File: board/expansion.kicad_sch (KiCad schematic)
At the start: 1 part, among them J7 Conn_02x32_Counter_Clockwise

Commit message: design draft complete, added footprints
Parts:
- J7: footprint (none) -> Connector_PinHeader_2.54mm:PinHeader_2x32_P2.54mm_Vertical
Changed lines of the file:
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@@
 			)
 		)
-		(property "Footprint" ""
+		(property "Footprint" "Connector_PinHeader_2.54mm:PinHeader_2x32_P2.54mm_Vertical"
 			(at 97.79 73.66 0)
 			(effects

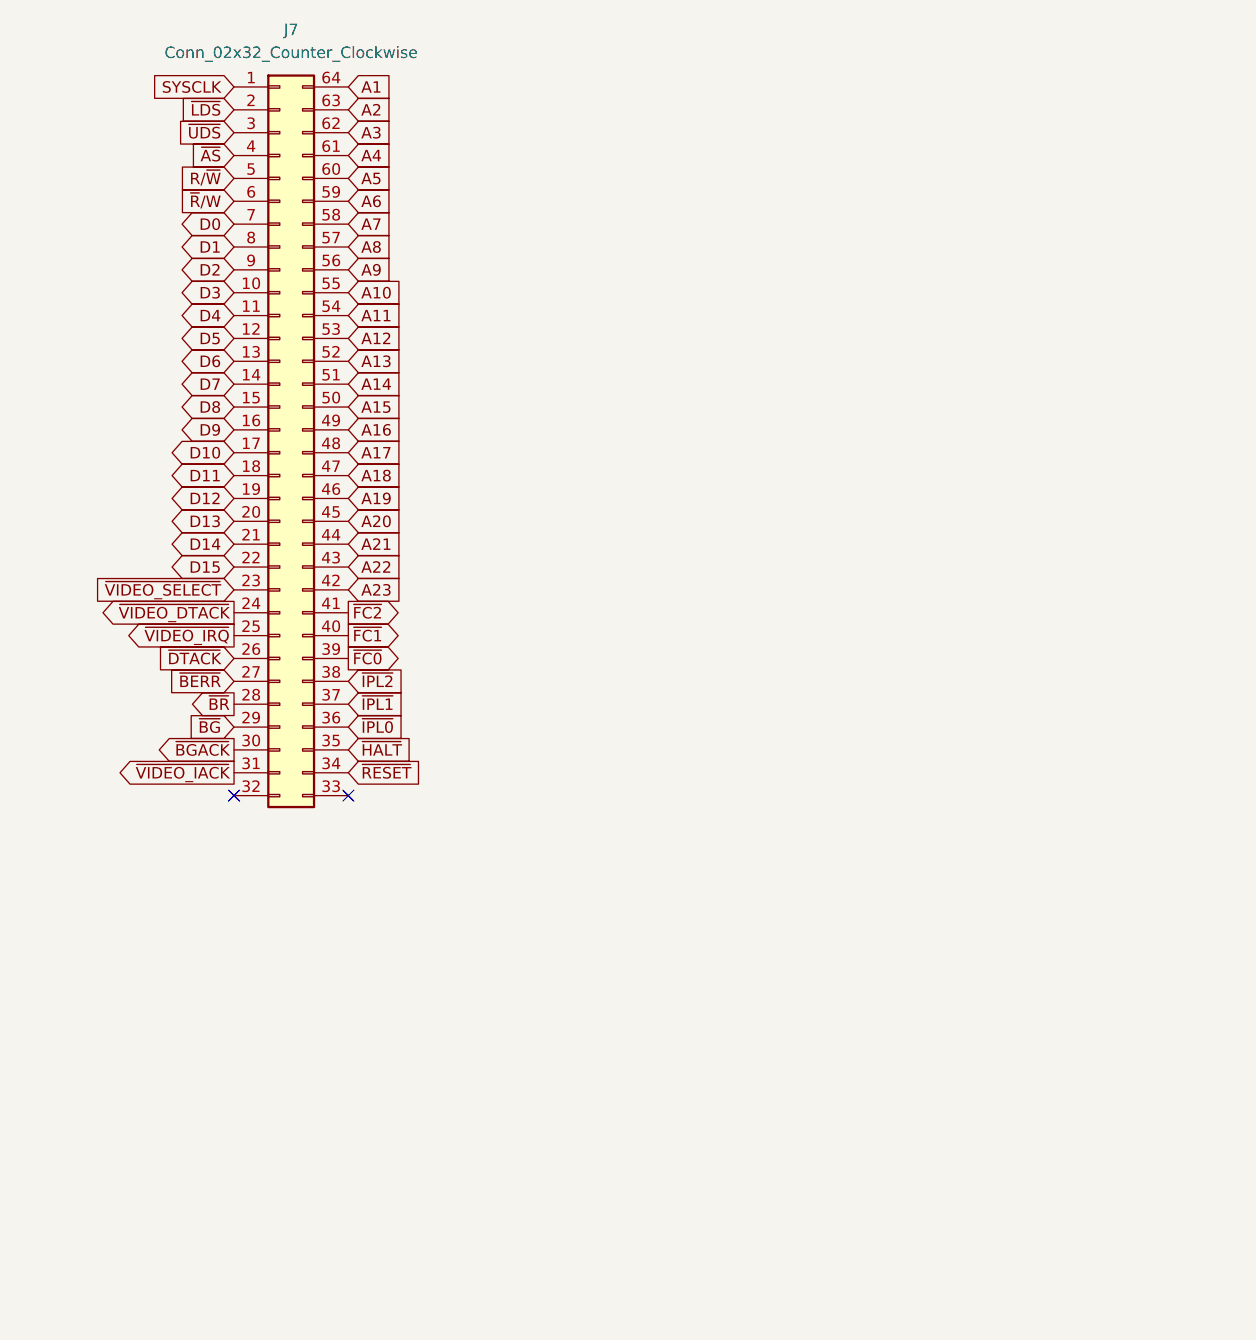
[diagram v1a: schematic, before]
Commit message: start of PCB and MMU
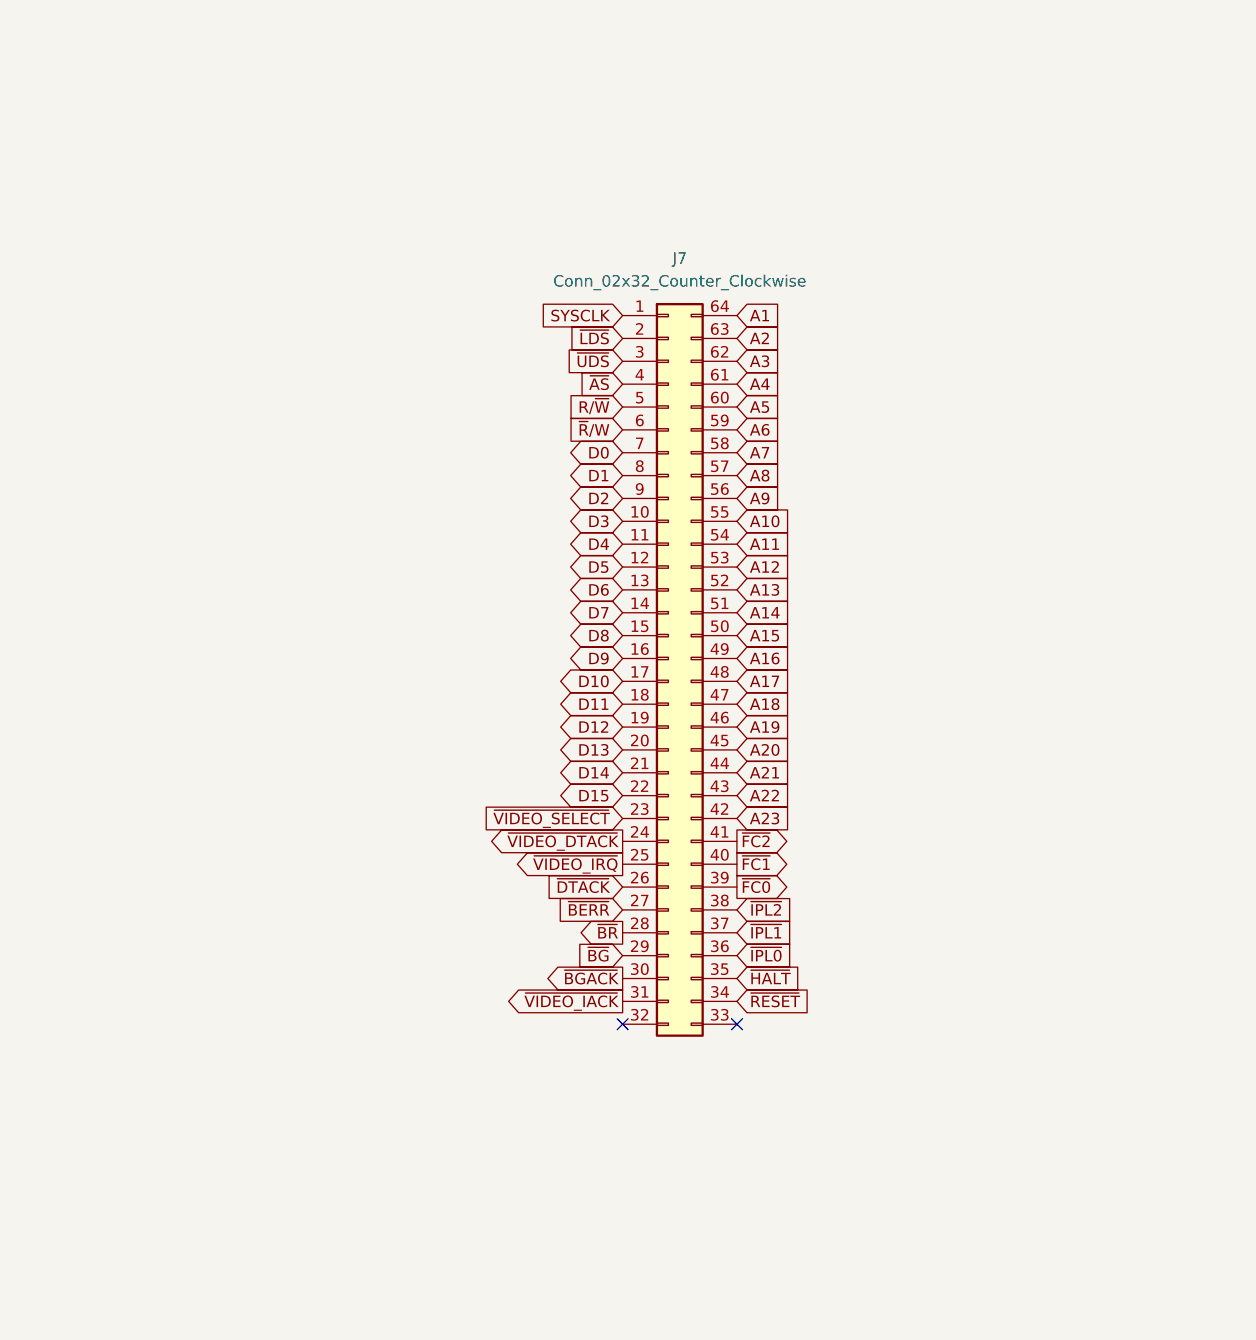
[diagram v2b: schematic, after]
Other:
- moved on the sheet: J7

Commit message: checkpoint
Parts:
- added H5, H6, H7, H8: MountingHole_Pad, MountingHole:MountingHole_2.5mm_Pad, symbol Mechanical:MountingHole_Pad
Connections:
- new net GND: H5.1, H6.1, H7.1, H8.1

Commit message: checkpoint - maybe unfinishable
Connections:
- net VIDEO_PRESENT: now reaches J7.32 (Pin_32)
- no-connect marks 2 -> 1
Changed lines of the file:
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@@
 		(at 148.59 139.7)
-	)
-	(no_connect
-		(at 135.89 139.7)
 	)
 	(global_label "D2"
@@
 				(hide yes)
 			)
+		)
+	)
+	(global_label "VIDEO_PRESENT"
+		(shape output)
+		(at 135.89 139.7 180)
+		(fields_autoplaced yes)
+		(effects
+			(font
+				(size 1.27 1.27)
+			)
+			(justify right)
+		)
+		(property "Intersheetrefs" "${INTERSHEET_REFS}"
+			(at 118.1487 139.7 0)
+			(effects
+				(font
+					(size 1.27 1.27)
+				)
+				(justify right)
+				(hide yes)
+			)

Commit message: checkpoint before reordering 1508 inputs
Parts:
- removed H5, H8: MountingHole_Pad, MountingHole:MountingHole_2.5mm_Pad, symbol Mechanical:MountingHole_Pad
- H6, H7: footprint MountingHole:MountingHole_2.5mm_Pad -> MountingHole:MountingHole_2.5mm_Pad_Via
- J7: value Conn_02x32_Counter_Clockwise -> Expansion Bus; footprint Connector_PinHeader_2.54mm:PinHeader_2x32_P2.54mm_Vertical -> Connector_PinHeader_2.54mm:PinHeader_2x36_P2.54mm_Vertical; symbol Connector_Generic:Conn_02x32_Counter_Clockwise -> Connector_Generic:Conn_02x36_Odd_Even
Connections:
- net A1: now also J7.53 (Pin_53); no longer J7.64 (Pin_64)
- net A10: now also J7.56 (Pin_56); no longer J7.55 (Pin_55)
- net A12: now also J7.52 (Pin_52); no longer J7.53 (Pin_53)
- net A13: now also J7.50 (Pin_50); no longer J7.52 (Pin_52)
- net A14: now also J7.48 (Pin_48); no longer J7.51 (Pin_51)
- net A15: now also J7.46 (Pin_46); no longer J7.50 (Pin_50)
- net A16: now also J7.44 (Pin_44); no longer J7.49 (Pin_49)
- net A17: now also J7.42 (Pin_42); no longer J7.48 (Pin_48)
- net A18: now also J7.40 (Pin_40); no longer J7.47 (Pin_47)
- net A19: now also J7.38 (Pin_38); no longer J7.46 (Pin_46)
- net A2: now also J7.55 (Pin_55); no longer J7.63 (Pin_63)
- net A20: now also J7.36 (Pin_36); no longer J7.45 (Pin_45)
- net A21: now also J7.32 (Pin_32); no longer J7.44 (Pin_44)
- net A22: now also J7.30 (Pin_30); no longer J7.43 (Pin_43)
- net A23: now also J7.28 (Pin_28); no longer J7.42 (Pin_42)
- net A3: now also J7.57 (Pin_57); no longer J7.62 (Pin_62)
- net A4: now also J7.59 (Pin_59); no longer J7.61 (Pin_61)
- net A5: now also J7.66 (Pin_66); no longer J7.60 (Pin_60)
- net A6: now also J7.64 (Pin_64); no longer J7.59 (Pin_59)
- net A7: now also J7.62 (Pin_62); no longer J7.58 (Pin_58)
- net A8: now also J7.60 (Pin_60); no longer J7.57 (Pin_57)
- net A9: now also J7.58 (Pin_58); no longer J7.56 (Pin_56)
- net D0: now also J7.11 (Pin_11); no longer J7.7 (Pin_7)
- net D1: now also J7.9 (Pin_9); no longer J7.8 (Pin_8)
- net D10: now also J7.14 (Pin_14); no longer J7.17 (Pin_17)
- net D11: now also J7.16 (Pin_16); no longer J7.18 (Pin_18)
- net D12: now also J7.18 (Pin_18); no longer J7.19 (Pin_19)
- net D14: now also J7.22 (Pin_22); no longer J7.21 (Pin_21)
- net D15: now also J7.24 (Pin_24); no longer J7.22 (Pin_22)
- net D2: now also J7.7 (Pin_7); no longer J7.9 (Pin_9)
- net D3: now also J7.5 (Pin_5); no longer J7.10 (Pin_10)
- net D4: now also J7.3 (Pin_3); no longer J7.11 (Pin_11)
- net D5: now also J7.4 (Pin_4); no longer J7.12 (Pin_12)
- net D6: now also J7.6 (Pin_6); no longer J7.13 (Pin_13)
- net D7: now also J7.8 (Pin_8); no longer J7.14 (Pin_14)
- net D8: now also J7.10 (Pin_10); no longer J7.15 (Pin_15)
- net D9: now also J7.12 (Pin_12); no longer J7.16 (Pin_16)
- net GND: now also J7.26 (Pin_26), J7.33 (Pin_33)
- net R/~{W}: now also J7.19 (Pin_19); no longer J7.5 (Pin_5)
- net SYSCLK: now also J7.31 (Pin_31); no longer J7.1 (Pin_1)
- net VIDEO_PRESENT: now also J7.70 (Pin_70); no longer J7.32 (Pin_32)
- net ~{AS}: now also J7.13 (Pin_13); no longer J7.4 (Pin_4)
- net ~{BERR}: now also J7.39 (Pin_39); no longer J7.27 (Pin_27)
- net ~{BGACK}: now also J7.25 (Pin_25); no longer J7.30 (Pin_30)
- net ~{BG}: now also J7.23 (Pin_23); no longer J7.29 (Pin_29)
- net ~{BR}: now also J7.27 (Pin_27); no longer J7.28 (Pin_28)
- net ~{DTACK}: now also J7.67 (Pin_67); no longer J7.26 (Pin_26)
- net ~{FC0}: now also J7.51 (Pin_51); no longer J7.39 (Pin_39)
- net ~{FC1}: now also J7.49 (Pin_49); no longer J7.40 (Pin_40)
- net ~{FC2}: now also J7.47 (Pin_47); no longer J7.41 (Pin_41)
- net ~{IPL0}: now also J7.45 (Pin_45); no longer J7.36 (Pin_36)
- net ~{IPL1}: now also J7.43 (Pin_43); no longer J7.37 (Pin_37)
- net ~{IPL2}: now also J7.41 (Pin_41); no longer J7.38 (Pin_38)
- net ~{LDS}: now also J7.17 (Pin_17); no longer J7.2 (Pin_2)
- net ~{RESET}: now also J7.37 (Pin_37); no longer J7.34 (Pin_34)
- net ~{R}/W: now also J7.21 (Pin_21); no longer J7.6 (Pin_6)
- net ~{UDS}: now also J7.15 (Pin_15); no longer J7.3 (Pin_3)
- net ~{VIDEO_DTACK}: now also J7.63 (Pin_63); no longer J7.24 (Pin_24)
- net ~{VIDEO_IACK}: now also J7.68 (Pin_68); no longer J7.31 (Pin_31)
- net ~{VIDEO_IRQ}: now also J7.65 (Pin_65); no longer J7.25 (Pin_25)
- net ~{VIDEO_SELECT}: now also J7.61 (Pin_61); no longer J7.23 (Pin_23)
- new net +3V3: J7.1 (Pin_1), J7.2 (Pin_2)
- new net +5V: J7.29 (Pin_29), J7.34 (Pin_34)
- no-connect marks 1 -> 3

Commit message: CF card, composite, VGA
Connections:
- net +3V3: no longer names the net of J7.1 (Pin_1)
- net +3V3: no longer J7.2 (Pin_2)
- no-connect marks 3 -> 5
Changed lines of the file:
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@@
+	)
+	(no_connect
+		(at 125.73 48.26)
+	)
+	(no_connect
+		(at 113.03 48.26)
 	)
 	(no_connect
@@
 	(wire
 		(pts
-			(xy 99.06 48.26) (xy 113.03 48.26)
+			(xy 96.52 88.9) (xy 113.03 88.9)
 		)
 		(stroke
@@
 	(wire
 		(pts
-			(xy 96.52 88.9) (xy 113.03 88.9)
+			(xy 96.52 83.82) (xy 113.03 83.82)
 		)
 		(stroke
@@
 	(wire
 		(pts
-			(xy 96.52 83.82) (xy 113.03 83.82)
-		)
-		(stroke
-			(width 0)
-			(type default)
-		)
-	)
-	(wire
-		(pts
 			(xy 125.73 88.9) (xy 146.05 88.9)
-		)
-		(stroke
-			(width 0)
-			(type default)
-		)
-	)
-	(wire
-		(pts
-			(xy 125.73 48.26) (xy 137.16 48.26)
 		)
 		(stroke
@@
 	)
 	(symbol
-		(lib_id "power:+3V3")
-		(at 137.16 48.26 0)
-		(unit 1)
-		(exclude_from_sim no)
-		(in_bom yes)
-		(on_board yes)
-		(dnp no)
-		(fields_autoplaced yes)
-		(property "Reference" "#PWR0167"
-			(at 137.16 52.07 0)
-			(effects
-				(font
-					(size 1.27 1.27)
-				)
-				(hide yes)
-			)
-		)
-		(property "Value" "+3V3"
-			(at 137.16 43.18 0)
-			(effects
-				(font
-					(size 1.27 1.27)
-				)
-			)
-		)
-		(property "Footprint" ""
-			(at 137.16 48.26 0)
-			(effects
-				(font
-					(size 1.27 1.27)
-				)
-				(hide yes)
-			)
-		)
-		(property "Datasheet" ""
-			(at 137.16 48.26 0)
-			(effects
-				(font
-					(size 1.27 1.27)
-				)
-				(hide yes)
-			)
-		)
-		(property "Description" "Power symbol creates a global label with name \"+3V3\""
-			(at 137.16 48.26 0)
-			(effects
-				(font
-					(size 1.27 1.27)
-				)
-				(hide yes)
-			)
-		)
-		(pin "1"
-		)
-		(instances
-			(project "board"
-				(path "/afefa398-9f39-4b22-97f8-dae9b102df0d/a6ee04b7-7d16-47ea-9db5-ea25e69d73a5"
-					(reference "#PWR0167")
-					(unit 1)
-				)
-			)
-		)
-	)
-	(symbol
 		(lib_id "Mechanical:MountingHole_Pad")
 		(at 193.04 88.9 90)
@@
 					(unit 1)
 				)
-			)
-		)
-	)
-	(symbol
-		(lib_id "power:+3V3")
-		(at 99.06 48.26 0)
-		(unit 1)
-		(exclude_from_sim no)
-		(in_bom yes)
-		(on_board yes)
-		(dnp no)
-		(fields_autoplaced yes)
-		(property "Reference" "#PWR0166"
-			(at 99.06 52.07 0)
-			(effects
-				(font
-					(size 1.27 1.27)
-				)
-				(hide yes)
-			)
-		)
-		(property "Value" "+3V3"
-			(at 99.06 43.18 0)
-			(effects
-				(font
-					(size 1.27 1.27)
-				)
-			)
-		)
-		(property "Footprint" ""
-			(at 99.06 48.26 0)
-			(effects
-				(font
-					(size 1.27 1.27)
-				)
-				(hide yes)
-			)
-		)
-		(property "Datasheet" ""
-			(at 99.06 48.26 0)
-			(effects
-				(font
-					(size 1.27 1.27)
-				)
-				(hide yes)
-			)
-		)
-		(property "Description" "Power symbol creates a global label with name \"+3V3\""
-			(at 99.06 48.26 0)
-			(effects
-				(font
-					(size 1.27 1.27)
-				)
-				(hide yes)
-			)
-		)
-		(pin "1"
-		)
-		(instances
-			(project ""
-				(path "/afefa398-9f39-4b22-97f8-dae9b102df0d/a6ee04b7-7d16-47ea-9db5-ea25e69d73a5"
-					(reference "#PWR0166")
-					(unit 1)
-				)

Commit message: checkpoint
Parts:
- removed H6, H7: MountingHole_Pad, MountingHole:MountingHole_2.5mm_Pad_Via, symbol Mechanical:MountingHole_Pad
- removed J7: Expansion Bus, Connector_PinHeader_2.54mm:PinHeader_2x36_P2.54mm_Vertical, symbol Connector_Generic:Conn_02x36_Odd_Even
- added C18: 100nF, Capacitor_THT:C_Disc_D5.0mm_W2.5mm_P5.00mm, symbol Device:C
- added U13: ENGINE, Package_LCC:PLCC-84_THT-Socket, symbol CPLD_Microchip:ATF1508ASx-xxJx84
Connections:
- net +5V: now also C18.1, U13.13 (VCCIO), U13.26 (VCCIO), U13.3 (VCCINT), U13.38 (VCCIO), U13.43 (VCCINT), U13.53 (VCCIO), U13.66 (VCCIO), U13.78 (VCCIO)
- net A1: now also U13.48 (I/O)
- net A10: now also U13.39 (I/O)
- net A11: now also U13.37 (I/O)
- net A13: now also U13.36 (I/O)
- net A14: now also U13.75 (I/O)
- net A15: now also U13.74 (I/O)
- net A16: now also U13.56 (I/O)
- net A17: now also U13.57 (I/O)
- net A18: now also U13.31 (I/O)
- net A19: now also U13.30 (I/O)
- net A2: now also U13.49 (I/O)
- net A20: now also U13.58 (I/O)
- net A21: now also U13.28 (I/O)
- net A22: now also U13.60 (I/O)
- net A23: now also U13.61 (I/O)
- net A3: now also U13.51 (I/O)
- net A4: now also U13.54 (I/O)
- net A5: now also U13.55 (I/O)
- net A6: now also U13.52 (I/O)
- net A7: now also U13.50 (I/O)
- net A8: now also U13.45 (I/O/PD2)
- net A9: now also U13.44 (I/O)
- net D0: now also U13.18 (I/O)
- net D1: now also U13.68 (I/O)
- net D10: now also U13.67 (I/O)
- net D11: now also U13.20 (I/O)
- net D12: now also U13.65 (I/O)
- net D13: now also U13.24 (I/O)
- net D14: now also U13.63 (I/O)
- net D15: now also U13.27 (I/O)
- net D2: now also U13.17 (I/O)
- net D3: now also U13.15 (I/O)
- net D4: now also U13.12 (I/O/PD1)
- net D5: now also U13.11 (I/O)
- net D6: now also U13.73 (I/O)
- net D7: now also U13.70 (I/O)
- net D8: now also U13.16 (I/O)
- net D9: now also U13.69 (I/O)
- net GND: now also C18.2, U13.1 (INPUT/GCLR), U13.19 (GND), U13.32 (GND), U13.42 (GND), U13.47 (GND), U13.59 (GND), U13.7 (GND), U13.72 (GND), U13.82 (GND)
- net R/~{W}: now also U13.25 (I/O)
- net ~{AS}: now also U13.21 (I/O)
- net ~{BGACK}: now also U13.77 (I/O)
- net ~{BG}: now also U13.76 (I/O)
- net ~{BR}: now also U13.79 (I/O)
- net ~{DTACK}: now also U13.81 (I/O/GCLK3)
- net ~{FC0}: now also U13.33 (I/O)
- net ~{FC1}: now also U13.34 (I/O)
- net ~{FC2}: now also U13.35 (I/O)
- net ~{LDS}: now also U13.64 (I/O)
- net ~{RESET}: now also U13.41 (I/O)
- net ~{UDS}: now also U13.22 (I/O)
- new net CPUCLK: U13.83 (INPUT/GCLK1)
- new net ENGINE_TCK: U13.62 (I/O/TCK)
- new net ENGINE_TDI: U13.14 (I/O/TDI)
- new net ENGINE_TDO: U13.71 (I/O/TDO)
- new net ENGINE_TMS: U13.23 (I/O/TMS)
- new net ~{ENGINE_DTACK}: U13.4 (I/O)
- new net ~{ENGINE_IACK}: U13.6 (I/O)
- new net ~{ENGINE_IRQ}: U13.5 (I/O)
- new net ~{ENGINE_SELECT}: U13.84 (INPUT/OE1)
- no-connect marks 5 -> 8

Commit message: Board rev1 PCB complete, already have a spot fix
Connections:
- net GND: no longer U13.1 (INPUT/GCLR)
- net ~{RESET}: now also U13.1 (INPUT/GCLR); no longer U13.41 (I/O)
- net A12: now reaches U13.29 (I/O)
- net ~{FC0} renamed FC0
- net ~{FC1} renamed FC1
- net ~{FC2} renamed FC2
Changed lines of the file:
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@@
-	)
-	(no_connect
-		(at 91.44 105.41)
 	)
 	(no_connect
 		(at 137.16 130.81)
 	)
+	(no_connect
+		(at 91.44 133.35)
+	)
 	(wire
 		(pts
@@
 	(wire
 		(pts
-			(xy 72.39 138.43) (xy 72.39 148.59)
-		)
-		(stroke
-			(width 0)
-			(type default)
-		)
-	)
-	(wire
-		(pts
 			(xy 132.08 125.73) (xy 137.16 125.73)
 		)
@@
 	(wire
 		(pts
-			(xy 96.52 138.43) (xy 72.39 138.43)
-		)
-		(stroke
-			(width 0)
-			(type default)
-		)
-	)
-	(wire
-		(pts
 			(xy 91.44 59.69) (xy 96.52 59.69)
 		)
@@
 		(pts
 			(xy 91.44 97.79) (xy 96.52 97.79)
+		)
+		(stroke
+			(width 0)
+			(type default)
+		)
+	)
+	(wire
+		(pts
+			(xy 91.44 138.43) (xy 96.52 138.43)
 		)
 		(stroke
@@
 		)
 	)
+	(global_label "~{RESET}"
+		(shape input)
+		(at 91.44 138.43 180)
+		(fields_autoplaced yes)
+		(effects
+			(font
+				(size 1.27 1.27)
+			)
+			(justify right)
+		)
+		(property "Intersheetrefs" "${INTERSHEET_REFS}"
+			(at 82.7097 138.43 0)
+			(effects
+				(font
+					(size 1.27 1.27)
+				)
+				(justify right)
+				(hide yes)
+			)
+		)
+	)
 	(global_label "CPUCLK"
 		(shape input)
@@
 		)
 	)
-	(global_label "~{FC2}"
+	(global_label "FC2"
 		(shape input)
 		(at 91.44 120.65 180)
@@
 		)
 	)
+	(global_label "A12"
+		(shape bidirectional)
+		(at 91.44 105.41 180)
+		(fields_autoplaced yes)
+		(effects
+			(font
+				(size 1.27 1.27)
+			)
+			(justify right)
+		)
+		(property "Intersheetrefs" "${INTERSHEET_REFS}"
+			(at 83.8359 105.41 0)
+			(effects
+				(font
+					(size 1.27 1.27)
+				)
+				(justify right)
+				(hide yes)
+			)
+		)
+	)
 	(global_label "A11"
 		(shape bidirectional)
@@
 		)
 	)
-	(global_label "~{RESET}"
-		(shape input)
-		(at 91.44 133.35 180)
-		(fields_autoplaced yes)
-		(effects
-			(font
-				(size 1.27 1.27)
-			)
-			(justify right)
-		)
-		(property "Intersheetrefs" "${INTERSHEET_REFS}"
-			(at 82.7097 133.35 0)
-			(effects
-				(font
-					(size 1.27 1.27)
-				)
-				(justify right)
-				(hide yes)
-			)
-		)
-	)
 	(global_label "~{BR}"
 		(shape output)
@@
 		)
 	)
-	(global_label "~{FC1}"
+	(global_label "FC1"
 		(shape input)
 		(at 91.44 118.11 180)
@@
 		)
 	)
-	(global_label "~{FC0}"
+	(global_label "FC0"
 		(shape input)
 		(at 91.44 115.57 180)
@@
 					(unit 1)
 				)
-			)
-		)
-	)
-	(symbol
-		(lib_id "power:GND")
-		(at 72.39 148.59 0)
-		(unit 1)
-		(exclude_from_sim no)
-		(in_bom yes)
-		(on_board yes)
-		(dnp no)
-		(fields_autoplaced yes)
-		(property "Reference" "#PWR01"
-			(at 72.39 154.94 0)
-			(effects
-				(font
-					(size 1.27 1.27)
-				)
-				(hide yes)
-			)
-		)
-		(property "Value" "GND"
-			(at 72.39 153.67 0)
-			(effects
-				(font
-					(size 1.27 1.27)
-				)
-			)
-		)
-		(property "Footprint" ""
-			(at 72.39 148.59 0)
-			(effects
-				(font
-					(size 1.27 1.27)
-				)
-				(hide yes)
-			)
-		)
-		(property "Datasheet" ""
-			(at 72.39 148.59 0)
-			(effects
-				(font
-					(size 1.27 1.27)
-				)
-				(hide yes)
-			)
-		)
-		(property "Description" "Power symbol creates a global label with name \"GND\" , ground"
-			(at 72.39 148.59 0)
-			(effects
-				(font
-					(size 1.27 1.27)
-				)
-				(hide yes)
-			)
-		)
-		(pin "1"
-		)
-		(instances
-			(project "board"
-				(path "/afefa398-9f39-4b22-97f8-dae9b102df0d/a6ee04b7-7d16-47ea-9db5-ea25e69d73a5"
-					(reference "#PWR01")
-					(unit 1)
-				)
